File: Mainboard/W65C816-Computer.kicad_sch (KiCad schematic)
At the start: 77 parts, among them J1 ADDR_DATA_DBG, J2 CTRL_BANK_DBG, J3 CPU_MISC_DBG, J4 PJ-102A 5V_IN, J5 DAUGHTER_PWR_AUX, Q1 P-MOSFET_REV_PROT_TO220, SW1 RESET, SW2 NMI, SW3 MAIN_PWR_SW_EXT, U1 W65C816S6PG-14, U10 SN74HC04N, U2 SN74HC573N, U20 AS6C4008-55PCN, U3 SN74HC245N, U30 SST39VF040-70-4I-NHE, U4 MCP130-315D, U5 SN74HC14N, U6 SN74HC138N, U7 SN74HC138N, U9 SN74HC00N, X1 ECS-P143X-8.000-BN

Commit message: Add lock file for W65C816-Computer schematic with hostname and username
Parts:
- added C21, C22, C23, C24, C25, C26, C27: 100nF, Capacitor_THT:C_Disc_D3.0mm_W1.6mm_P2.50mm, symbol Device:C
- added J6: DAUGHTER_BUS_A, Connector_PinSocket_2.54mm:PinSocket_2x20_P2.54mm_Vertical, symbol Connector_Generic:Conn_02x20_Odd_Even
- added J7: DAUGHTER_BUS_B, Connector_PinSocket_2.54mm:PinSocket_2x20_P2.54mm_Vertical, symbol Connector_Generic:Conn_02x20_Odd_Even
- added U21, U22, U23, U24, U25, U26, U27: AS6C4008-55PCN, Package_DIP:DIP-32_W15.24mm_Socket_LongPads, symbol Memory_RAM:AS6C4008-55PCN
- F1: value 2.5A -> 5A
- J4: value PJ-102A 5V_IN -> PJ-102AH 5V_IN; footprint PJ-102A:CUI_PJ-102A -> Connector_BarrelJack:BarrelJack_CUI_PJ-102AH_Horizontal; Current Rating (none) -> 5A; MPN (none) -> PJ-102AH
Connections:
- net +3V3: now also C21.1, C22.1, C23.1, C24.1, C25.1, C26.1, C27.1, J6.2 (Pin_2), J6.20 (Pin_20), J7.2 (Pin_2), J7.38 (Pin_38), U21.32 (VCC), U22.32 (VCC), U23.32 (VCC), U24.32 (VCC), U25.32 (VCC), U26.32 (VCC), U27.32 (VCC)
- net +5V: now also J6.38 (Pin_38), J6.40 (Pin_40)
- net A0: now also J6.3 (Pin_3), U21.12 (A0), U22.12 (A0), U23.12 (A0), U24.12 (A0), U25.12 (A0), U26.12 (A0), U27.12 (A0)
- net A1: now also J6.5 (Pin_5), U21.11 (A1), U22.11 (A1), U23.11 (A1), U24.11 (A1), U25.11 (A1), U26.11 (A1), U27.11 (A1)
- net A10: now also J6.25 (Pin_25), U21.23 (A10), U22.23 (A10), U23.23 (A10), U24.23 (A10), U25.23 (A10), U26.23 (A10), U27.23 (A10)
- net A11: now also J6.27 (Pin_27), U21.25 (A11), U22.25 (A11), U23.25 (A11), U24.25 (A11), U25.25 (A11), U26.25 (A11), U27.25 (A11)
- net A12: now also J6.29 (Pin_29), U21.4 (A12), U22.4 (A12), U23.4 (A12), U24.4 (A12), U25.4 (A12), U26.4 (A12), U27.4 (A12)
- net A13: now also J6.31 (Pin_31), U21.28 (A13), U22.28 (A13), U23.28 (A13), U24.28 (A13), U25.28 (A13), U26.28 (A13), U27.28 (A13)
- net A14: now also J6.33 (Pin_33), U21.3 (A14), U22.3 (A14), U23.3 (A14), U24.3 (A14), U25.3 (A14), U26.3 (A14), U27.3 (A14)
- net A15: now also J6.35 (Pin_35), U21.31 (A15), U22.31 (A15), U23.31 (A15), U24.31 (A15), U25.31 (A15), U26.31 (A15), U27.31 (A15)
- net A16: now also J6.22 (Pin_22), U21.2 (A16), U22.2 (A16), U23.2 (A16), U24.2 (A16), U25.2 (A16), U26.2 (A16), U27.2 (A16)
- net A17: now also J6.24 (Pin_24), U21.30 (A17), U22.30 (A17), U23.30 (A17), U24.30 (A17), U25.30 (A17), U26.30 (A17), U27.30 (A17)
- net A18: now also J6.26 (Pin_26), U21.1 (A18), U22.1 (A18), U23.1 (A18), U24.1 (A18), U25.1 (A18), U26.1 (A18), U27.1 (A18)
- net A19: now also J6.28 (Pin_28)
- net A2: now also J6.7 (Pin_7), U21.10 (A2), U22.10 (A2), U23.10 (A2), U24.10 (A2), U25.10 (A2), U26.10 (A2), U27.10 (A2)
- net A20: now also J6.30 (Pin_30)
- net A21: now also J6.32 (Pin_32)
- net A22: now also J6.34 (Pin_34)
- net A23: now also J6.36 (Pin_36)
- net A3: now also J6.9 (Pin_9), U21.9 (A3), U22.9 (A3), U23.9 (A3), U24.9 (A3), U25.9 (A3), U26.9 (A3), U27.9 (A3)
- net A4: now also J6.11 (Pin_11), U21.8 (A4), U22.8 (A4), U23.8 (A4), U24.8 (A4), U25.8 (A4), U26.8 (A4), U27.8 (A4)
- net A5: now also J6.13 (Pin_13), U21.7 (A5), U22.7 (A5), U23.7 (A5), U24.7 (A5), U25.7 (A5), U26.7 (A5), U27.7 (A5)
- net A6: now also J6.15 (Pin_15), U21.6 (A6), U22.6 (A6), U23.6 (A6), U24.6 (A6), U25.6 (A6), U26.6 (A6), U27.6 (A6)
- net A7: now also J6.17 (Pin_17), U21.5 (A7), U22.5 (A7), U23.5 (A7), U24.5 (A7), U25.5 (A7), U26.5 (A7), U27.5 (A7)
- net A8: now also J6.21 (Pin_21), U21.27 (A8), U22.27 (A8), U23.27 (A8), U24.27 (A8), U25.27 (A8), U26.27 (A8), U27.27 (A8)
- net A9: now also J6.23 (Pin_23), U21.26 (A9), U22.26 (A9), U23.26 (A9), U24.26 (A9), U25.26 (A9), U26.26 (A9), U27.26 (A9)
- net ABORT_N: now also J7.12 (Pin_12)
- net BANK00: now also J7.17 (Pin_17)
- net BANK00_N: now also J7.18 (Pin_18)
- net BE: now also J7.11 (Pin_11)
- net E: now also J7.15 (Pin_15)
- net GND: now also C21.2, C22.2, C23.2, C24.2, C25.2, C26.2, C27.2, J6.1 (Pin_1), J6.19 (Pin_19), J6.37 (Pin_37), J6.39 (Pin_39), J7.1 (Pin_1), J7.37 (Pin_37), J7.40 (Pin_40), U21.16 (VSS), U22.16 (VSS), U23.16 (VSS), U24.16 (VSS), U25.16 (VSS), U26.16 (VSS), U27.16 (VSS)
- net IRQ_N: now also J7.7 (Pin_7)
- net MEM_OE_N: now also J7.19 (Pin_19), U21.24 (OE#), U22.24 (OE#), U23.24 (OE#), U24.24 (OE#), U25.24 (OE#), U26.24 (OE#), U27.24 (OE#)
- net MEM_WE_N: now also J7.20 (Pin_20), U21.29 (WE#), U22.29 (WE#), U23.29 (WE#), U24.29 (WE#), U25.29 (WE#), U26.29 (WE#), U27.29 (WE#)
- net MLB: now also J7.14 (Pin_14)
- net MX: now also J7.16 (Pin_16)
- net NMI_N: now also J7.8 (Pin_8)
- net PHI2: now also J7.3 (Pin_3)
- net RAM_BLOCK0_N: now also J7.22 (Pin_22)
- net RAM_CS1_N: now also U21.22 (CE#)
- net RAM_CS2_N: now also U22.22 (CE#)
- net RAM_CS3_N: now also U23.22 (CE#)
- net RAM_CS4_N: now also U24.22 (CE#)
- net RAM_CS5_N: now also U25.22 (CE#)
- net RAM_CS6_N: now also U26.22 (CE#)
- net RAM_CS7_N: now also U27.22 (CE#)
- net RDY: now also J7.6 (Pin_6)
- net RESET_N: now also J7.5 (Pin_5)
- net ROM_CS_N: now also J7.21 (Pin_21)
- net RWB: now also J7.4 (Pin_4)
- net SYS_D0: now also J6.4 (Pin_4), U21.13 (DQ0), U22.13 (DQ0), U23.13 (DQ0), U24.13 (DQ0), U25.13 (DQ0), U26.13 (DQ0), U27.13 (DQ0)
- net SYS_D1: now also J6.6 (Pin_6), U21.14 (DQ1), U22.14 (DQ1), U23.14 (DQ1), U24.14 (DQ1), U25.14 (DQ1), U26.14 (DQ1), U27.14 (DQ1)
- net SYS_D2: now also J6.8 (Pin_8), U21.15 (DQ2), U22.15 (DQ2), U23.15 (DQ2), U24.15 (DQ2), U25.15 (DQ2), U26.15 (DQ2), U27.15 (DQ2)
- net SYS_D3: now also J6.10 (Pin_10), U21.17 (DQ3), U22.17 (DQ3), U23.17 (DQ3), U24.17 (DQ3), U25.17 (DQ3), U26.17 (DQ3), U27.17 (DQ3)
- net SYS_D4: now also J6.12 (Pin_12), U21.18 (DQ4), U22.18 (DQ4), U23.18 (DQ4), U24.18 (DQ4), U25.18 (DQ4), U26.18 (DQ4), U27.18 (DQ4)
- net SYS_D5: now also J6.14 (Pin_14), U21.19 (DQ5), U22.19 (DQ5), U23.19 (DQ5), U24.19 (DQ5), U25.19 (DQ5), U26.19 (DQ5), U27.19 (DQ5)
- net SYS_D6: now also J6.16 (Pin_16), U21.20 (DQ6), U22.20 (DQ6), U23.20 (DQ6), U24.20 (DQ6), U25.20 (DQ6), U26.20 (DQ6), U27.20 (DQ6)
- net SYS_D7: now also J6.18 (Pin_18), U21.21 (DQ7), U22.21 (DQ7), U23.21 (DQ7), U24.21 (DQ7), U25.21 (DQ7), U26.21 (DQ7), U27.21 (DQ7)
- net VDA: now also J7.9 (Pin_9)
- net VPA: now also J7.10 (Pin_10)
- net VPB: now also J7.13 (Pin_13)
- new net AUDIO_IRQ: J7.31 (Pin_31)
- new net DB_GPIO0: J7.34 (Pin_34)
- new net DB_GPIO1: J7.35 (Pin_35)
- new net DB_GPIO2: J7.36 (Pin_36)
- new net DB_GPIO3: J7.39 (Pin_39)
- new net DMA_ACK: J7.28 (Pin_28)
- new net DMA_REQ: J7.27 (Pin_27)
- new net EXP_CS_N: J7.33 (Pin_33)
- new net FRAME_IRQ: J7.30 (Pin_30)
- new net IO_CS_N: J7.24 (Pin_24)
- new net IO_IRQ: J7.32 (Pin_32)
- new net IO_RD_N: J7.25 (Pin_25)
- new net IO_WR_N: J7.26 (Pin_26)
- new net ROM_OVERLAY: J7.29 (Pin_29)
- new net RP_CS_N: J7.23 (Pin_23)
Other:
- note added: "SRAM sockets U21-U27 complete 4 MB main SRAM bank with U20"

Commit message: Refactor code structure for improved readability and maintainability
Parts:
- J4: value PJ-102AH 5V_IN -> PJ-102A; footprint Connector_BarrelJack:BarrelJack_CUI_PJ-102AH_Horizontal -> PJ-102A:CUI_PJ-102A; AVAILABILITY (none) -> Good; MANUFACTURER (none) -> CUI inc; MF (none) -> CUI; MP (none) -> PJ-102A; PACKAGE (none) -> None; PRICE (none) -> 0.44 USD

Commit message: Added 74HC138 74HC139
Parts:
- added C60, C61, C62: 100nF, Capacitor_THT:C_Disc_D3.0mm_W1.6mm_P2.50mm, symbol Device:C
- added TP26: RP_CS_N, TestPoint:TestPoint_THTPad_D1.5mm_Drill0.7mm, symbol Connector:TestPoint
- added TP27: IO_CS_N, TestPoint:TestPoint_THTPad_D1.5mm_Drill0.7mm, symbol Connector:TestPoint
- added TP28: EXP_CS_N, TestPoint:TestPoint_THTPad_D1.5mm_Drill0.7mm, symbol Connector:TestPoint
- added TP29: IO_RD_N, TestPoint:TestPoint_THTPad_D1.5mm_Drill0.7mm, symbol Connector:TestPoint
- added TP30: IO_WR_N, TestPoint:TestPoint_THTPad_D1.5mm_Drill0.7mm, symbol Connector:TestPoint
- added U11: SN74HC08N, Package_DIP:DIP-14_W7.62mm_Socket_LongPads, symbol 74xx:74LS08
- added U12: SN74HC139N, Package_DIP:DIP-16_W7.62mm_Socket_LongPads, symbol 74xx:74LS139
- added U8: SN74HC138N, Package_DIP:DIP-16_W7.62mm_Socket_LongPads, symbol 74xx:74HC138
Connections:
- net +3V3: now also C60.1, C61.1, C62.1, U11.14 (VCC), U12.16 (VCC), U8.16 (VCC)
- net A17: now also U8.1 (A0)
- net A18: now also U8.2 (A1)
- net A19: now also U8.3 (A2)
- net A20: now also U11.5
- net A21: now also U11.4
- net A22: now also U11.2
- net A23: now also U11.1
- net EXP_CS_N: now also TP28.1, U8.14 (~{Y1})
- net GND: now also C60.2, C61.2, C62.2, U11.12, U11.13, U11.7 (GND), U12.13 (A1), U12.14 (A0), U12.8 (GND), U8.4 (~{E0}), U8.5 (~{E1}), U8.8 (GND)
- net IO_CS_N: now also TP27.1, U12.1 (E), U12.15 (E), U8.15 (~{Y0})
- net IO_RD_N: now also TP29.1, U12.7 (O3)
- net IO_WR_N: now also TP30.1, U12.6 (O2)
- net PHI2: now also U12.3 (A1)
- net RP_CS_N: now also TP26.1, U12.12 (O0)
- net RWB: now also U12.2 (A0)
- new net F_A21_A20: U11.10, U11.6
- new net F_A23_A22: U11.3, U11.9
- new net F_HIGH: U11.8, U8.6 (E2)
- no-connect marks 17 -> 29

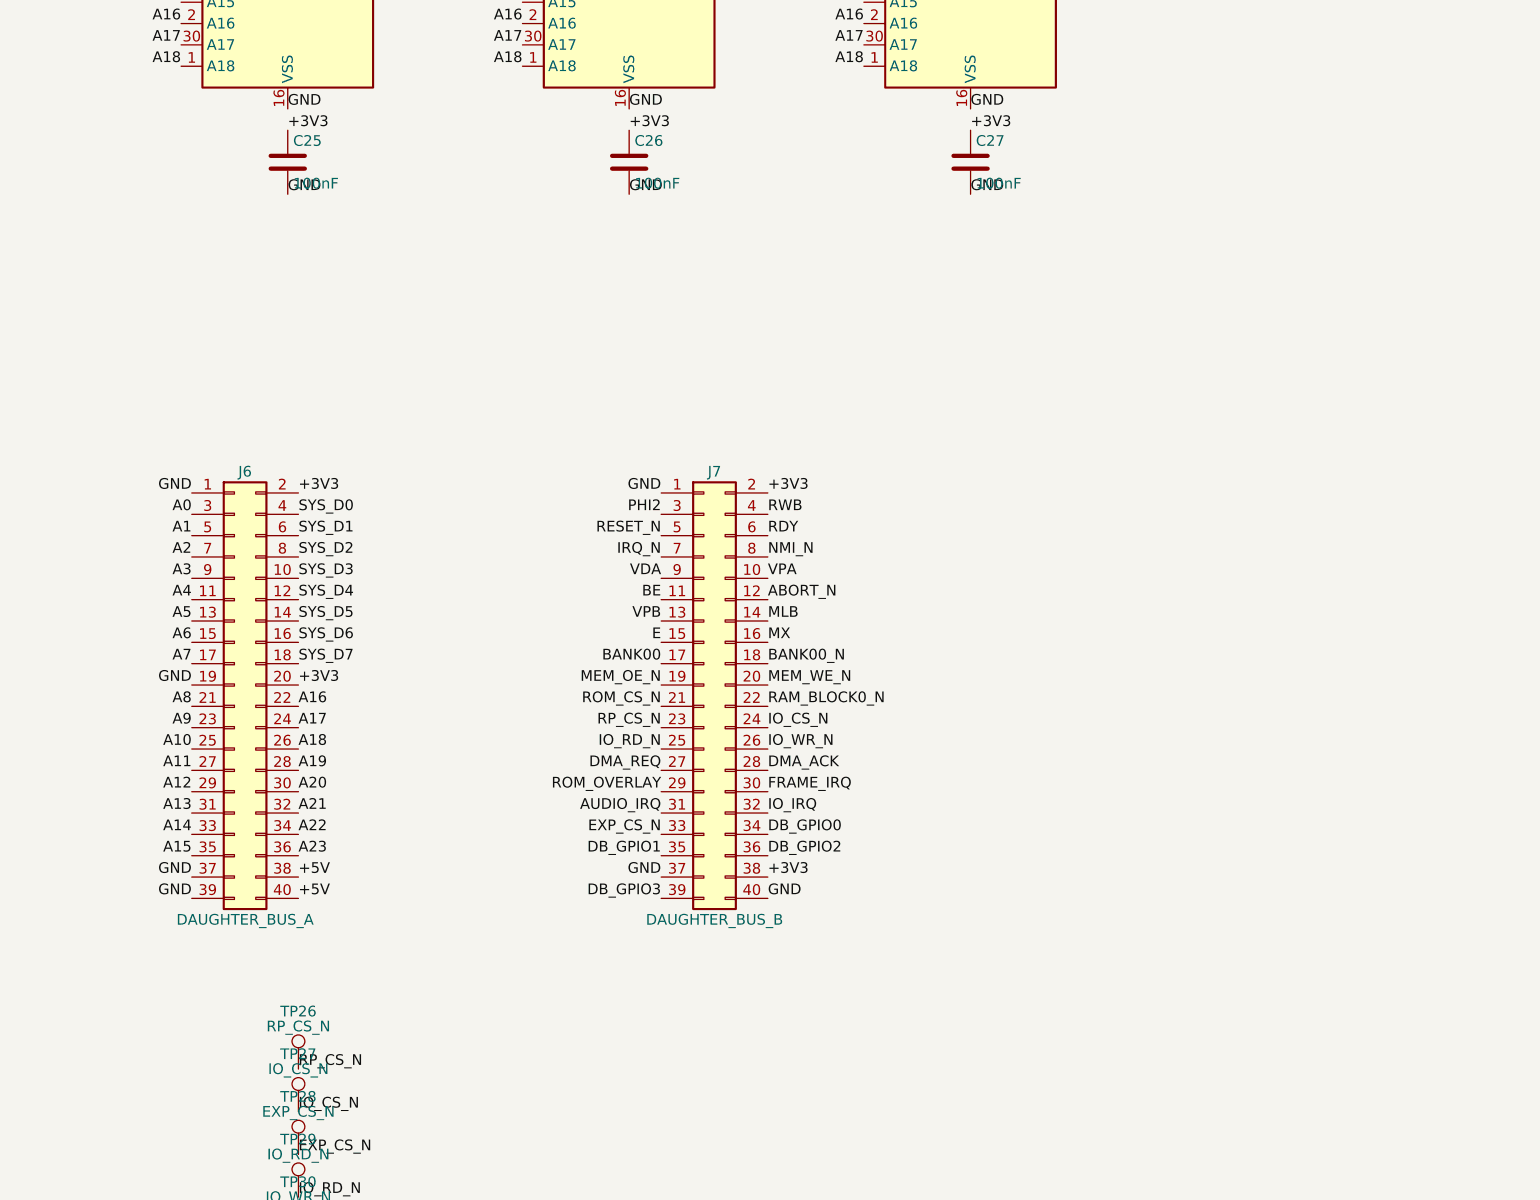
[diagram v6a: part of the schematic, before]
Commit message: Add CardEdge EDAC 395 footprint and update library table
- Created a new footprint for the CardEdge EDAC 395 2x40 P2.54mm Vertical THT connector in the W65C816-Computer.pretty library.
- Added the footprint to the fp-lib-table for easy access in KiCad.
- Documented the W65C816/RP2350 interface plan, outlining architecture, memory mapping, data bus contracts, interrupt architecture, and implementation sequence for revision A.
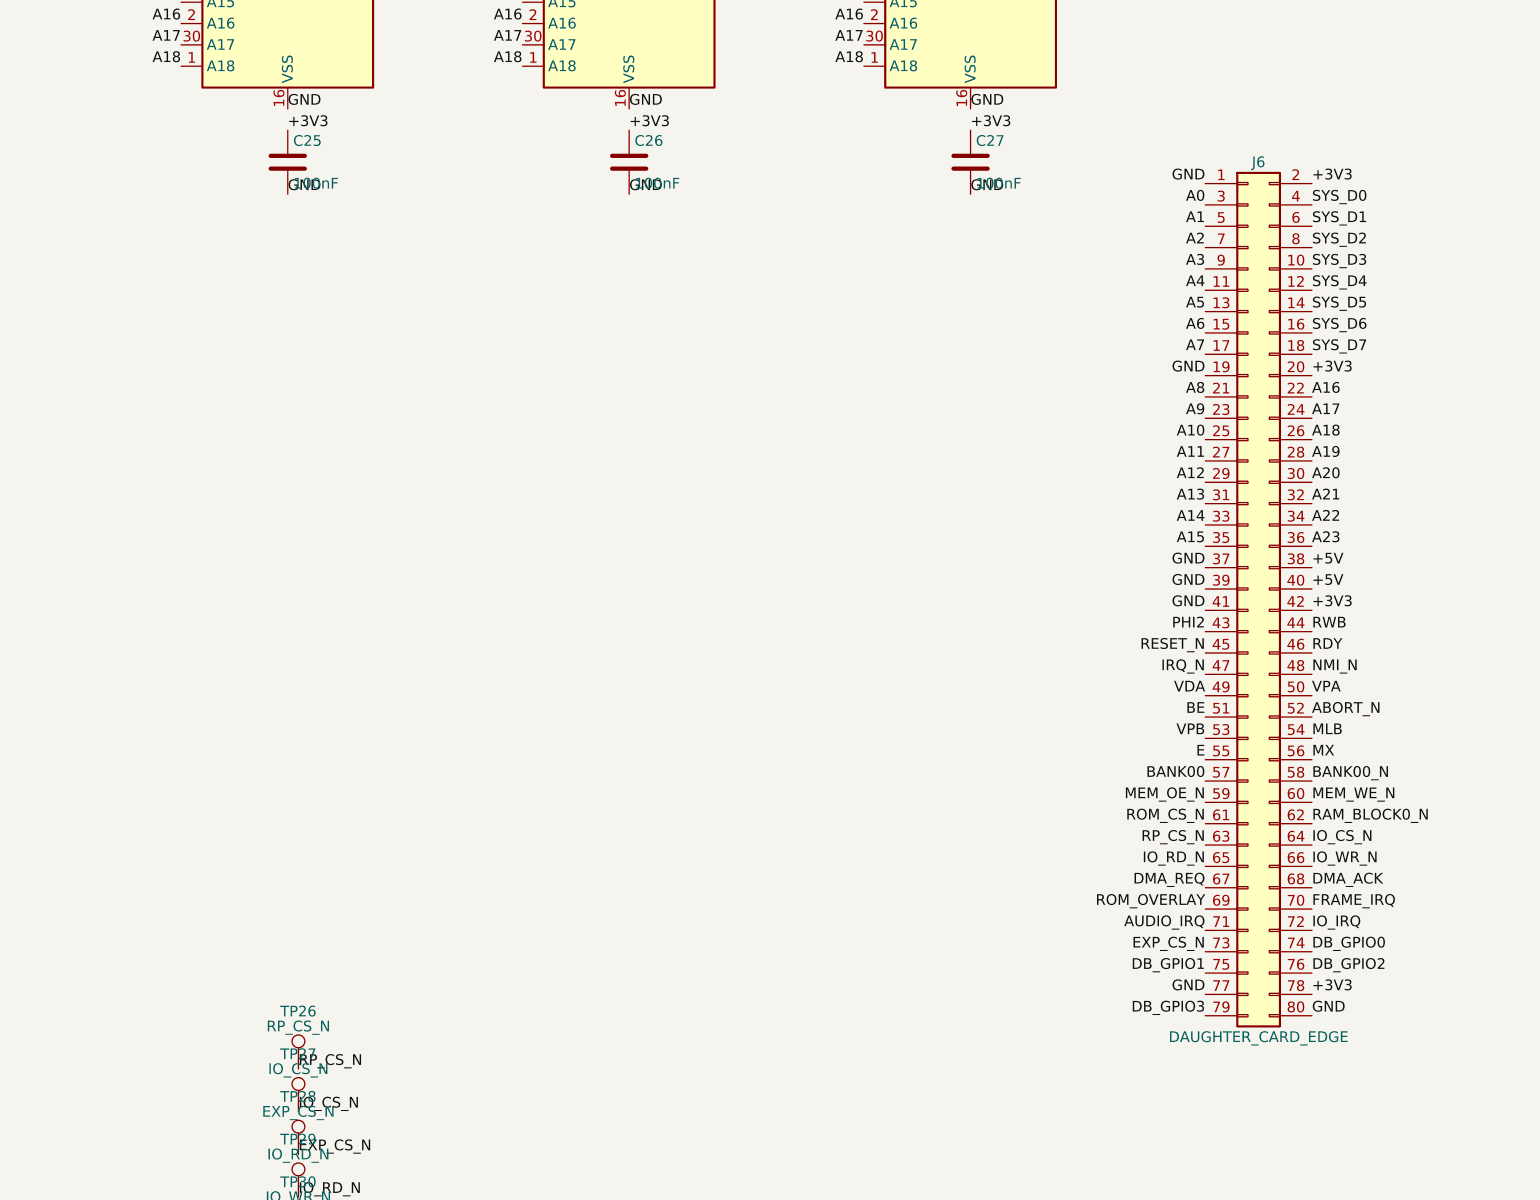
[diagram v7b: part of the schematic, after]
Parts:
- removed J6: DAUGHTER_BUS_A, Connector_PinSocket_2.54mm:PinSocket_2x20_P2.54mm_Vertical, symbol Connector_Generic:Conn_02x20_Odd_Even
- removed J7: DAUGHTER_BUS_B, Connector_PinSocket_2.54mm:PinSocket_2x20_P2.54mm_Vertical, symbol Connector_Generic:Conn_02x20_Odd_Even
- added J6: DAUGHTER_CARD_EDGE, 80_Standard_Edge_Conn:TE_2-5530843-0, symbol Connector_Generic:Conn_02x40_Odd_Even
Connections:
- net +3V3: now also J6.2 (Pin_2), J6.20 (Pin_20), J6.42 (Pin_42), J6.78 (Pin_78)
- net +5V: now also J6.38 (Pin_38), J6.40 (Pin_40)
- net A0: now also J6.3 (Pin_3)
- net A1: now also J6.5 (Pin_5)
- net A10: now also J6.25 (Pin_25)
- net A11: now also J6.27 (Pin_27)
- net A12: now also J6.29 (Pin_29)
- net A13: now also J6.31 (Pin_31)
- net A14: now also J6.33 (Pin_33)
- net A15: now also J6.35 (Pin_35)
- net A16: now also J6.22 (Pin_22)
- net A17: now also J6.24 (Pin_24)
- net A18: now also J6.26 (Pin_26)
- net A19: now also J6.28 (Pin_28)
- net A2: now also J6.7 (Pin_7)
- net A20: now also J6.30 (Pin_30)
- net A21: now also J6.32 (Pin_32)
- net A22: now also J6.34 (Pin_34)
- net A23: now also J6.36 (Pin_36)
- net A3: now also J6.9 (Pin_9)
- net A4: now also J6.11 (Pin_11)
- net A5: now also J6.13 (Pin_13)
- net A6: now also J6.15 (Pin_15)
- net A7: now also J6.17 (Pin_17)
- net A8: now also J6.21 (Pin_21)
- net A9: now also J6.23 (Pin_23)
- net ABORT_N: now also J6.52 (Pin_52)
- net AUDIO_IRQ: now also J6.71 (Pin_71)
- net BANK00: now also J6.57 (Pin_57)
- net BANK00_N: now also J6.58 (Pin_58)
- net BE: now also J6.51 (Pin_51)
- net DB_GPIO0: now also J6.74 (Pin_74)
- net DB_GPIO1: now also J6.75 (Pin_75)
- net DB_GPIO2: now also J6.76 (Pin_76)
- net DB_GPIO3: now also J6.79 (Pin_79)
- net DMA_ACK: now also J6.68 (Pin_68)
- net DMA_REQ: now also J6.67 (Pin_67)
- net E: now also J6.55 (Pin_55)
- net EXP_CS_N: now also J6.73 (Pin_73)
- net FRAME_IRQ: now also J6.70 (Pin_70)
- net GND: now also J6.1 (Pin_1), J6.19 (Pin_19), J6.37 (Pin_37), J6.39 (Pin_39), J6.41 (Pin_41), J6.77 (Pin_77), J6.80 (Pin_80)
- net IO_CS_N: now also J6.64 (Pin_64)
- net IO_IRQ: now also J6.72 (Pin_72)
- net IO_RD_N: now also J6.65 (Pin_65)
- net IO_WR_N: now also J6.66 (Pin_66)
- net IRQ_N: now also J6.47 (Pin_47)
- net MEM_OE_N: now also J6.59 (Pin_59)
- net MEM_WE_N: now also J6.60 (Pin_60)
- net MLB: now also J6.54 (Pin_54)
- net MX: now also J6.56 (Pin_56)
- net NMI_N: now also J6.48 (Pin_48)
- net PHI2: now also J6.43 (Pin_43)
- net RAM_BLOCK0_N: now also J6.62 (Pin_62)
- net RDY: now also J6.46 (Pin_46)
- net RESET_N: now also J6.45 (Pin_45)
- net ROM_CS_N: now also J6.61 (Pin_61)
- net ROM_OVERLAY: now also J6.69 (Pin_69)
- net RP_CS_N: now also J6.63 (Pin_63)
- net RWB: now also J6.44 (Pin_44)
- net SYS_D0: now also J6.4 (Pin_4)
- net SYS_D1: now also J6.6 (Pin_6)
- net SYS_D2: now also J6.8 (Pin_8)
- net SYS_D3: now also J6.10 (Pin_10)
- net SYS_D4: now also J6.12 (Pin_12)
- net SYS_D5: now also J6.14 (Pin_14)
- net SYS_D6: now also J6.16 (Pin_16)
- net SYS_D7: now also J6.18 (Pin_18)
- net VDA: now also J6.49 (Pin_49)
- net VPA: now also J6.50 (Pin_50)
- net VPB: now also J6.53 (Pin_53)

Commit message: Add ISA16 Slot footprint and mainboard PCB file
- Introduced a new footprint for the ISA16 Slot, including detailed pad specifications and dimensions.
- Added the W65C816-Computer.kicad_pcb.zip file containing the mainboard PCB design.
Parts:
- J6: value DAUGHTER_CARD_EDGE -> ISA16_DAUGHTER_BUS; footprint 80_Standard_Edge_Conn:TE_2-5530843-0 -> W65C816_Connector:ISA16_Slot; symbol Connector_Generic:Conn_02x40_Odd_Even -> W65C816-Computer:ISA16_DAUGHTER_BUS_98
- U20, U21, U22, U23: value AS6C4008-55PCN -> AS6C1008-55PCN
- U24, U25, U26, U27: footprint Package_DIP:DIP-32_W15.24mm_Socket_LongPads -> (none)
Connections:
- no-connect marks 29 -> 47
